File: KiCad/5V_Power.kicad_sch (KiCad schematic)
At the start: 24 parts, among them U4 NCP1117-3.3_SOT223, U5 XPS62912RPUR

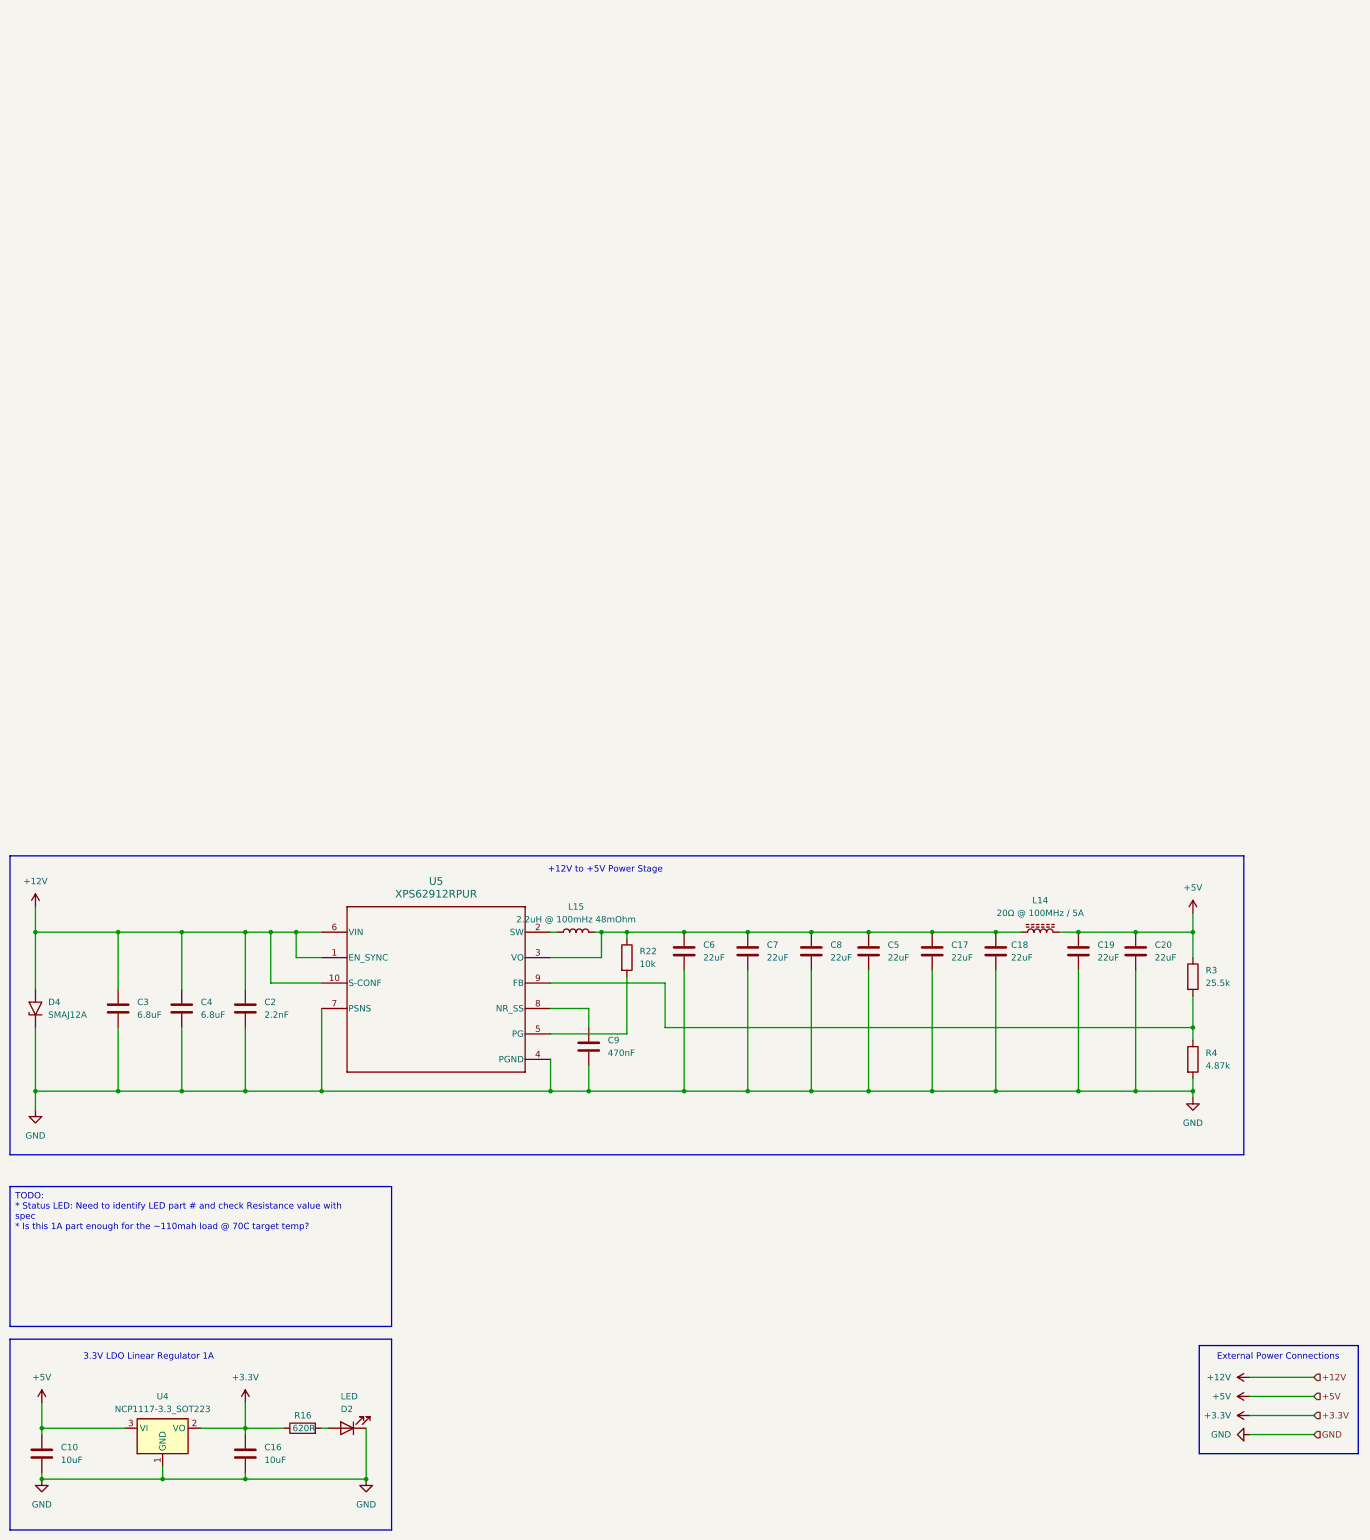
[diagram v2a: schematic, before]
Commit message: Convert Power to LDOs
Convert power section to use only LDOs. This means we will only get 4.75V or 4.5V on the analog line but this comes with greatly increased simplicity of layout.
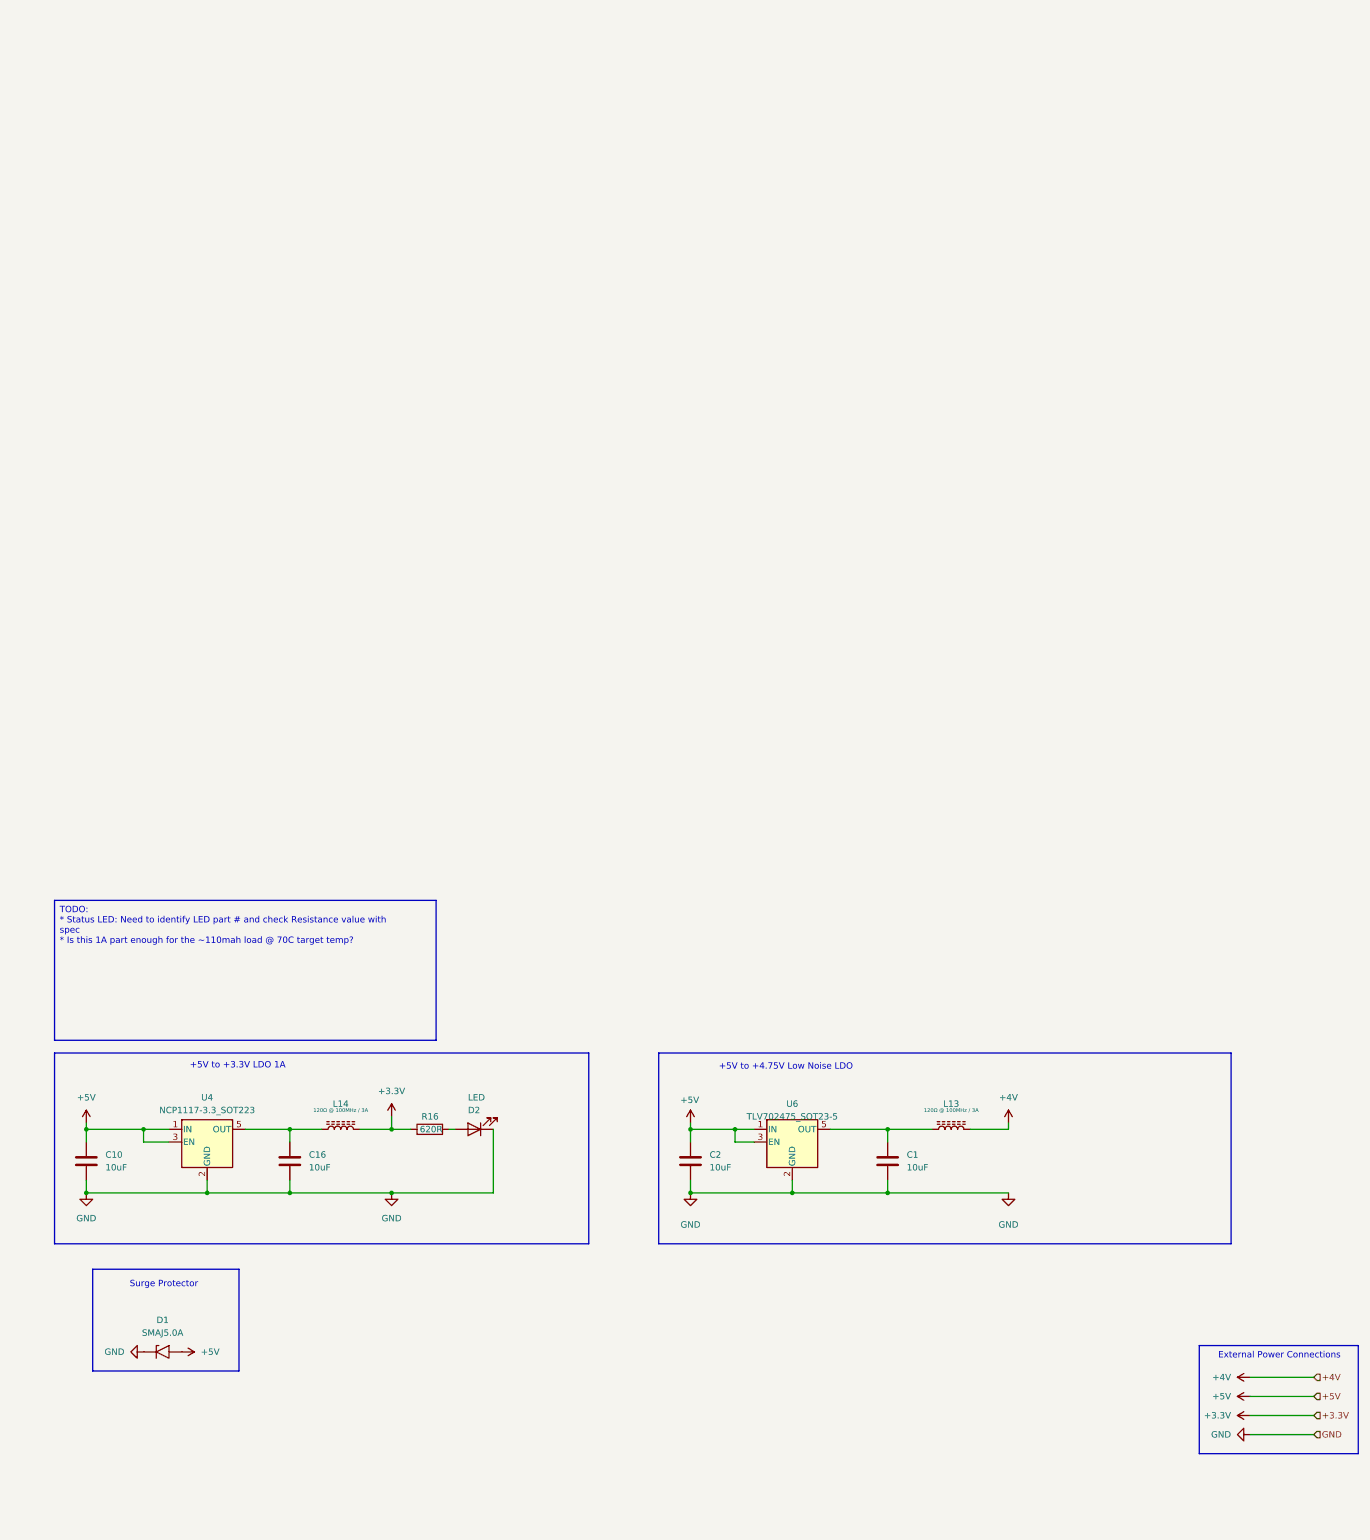
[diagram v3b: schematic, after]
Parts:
- removed C17, C18, C19, C20, C5, C6, C7, C8: 22uF, Capacitor_SMD:C_0805_2012Metric_Pad1.18x1.45mm_HandSolder, symbol Device:C
- removed C3, C4: 6.8uF, Capacitor_SMD:C_0805_2012Metric_Pad1.18x1.45mm_HandSolder, symbol Device:C
- removed C9: 470nF, Capacitor_SMD:C_0805_2012Metric_Pad1.18x1.45mm_HandSolder, symbol Device:C
- removed D4: SMAJ12A, Diode_SMD:D_SMA, symbol Diode:SMAJ12A
- removed L15: 2.2uH @ 100mHz 48mOhm, Inductor_SMD:L_Pulse_PA4320, symbol Device:L
- removed R22: 10k, Resistor_SMD:R_0805_2012Metric_Pad1.20x1.40mm_HandSolder, symbol Device:R
- removed R3: 25.5k, Resistor_SMD:R_0805_2012Metric_Pad1.20x1.40mm_HandSolder, symbol Device:R
- removed R4: 4.87k, Resistor_SMD:R_0805_2012Metric_Pad1.20x1.40mm_HandSolder, symbol Device:R
- removed U5: XPS62912RPUR, RPU0010A-MFG, symbol TPS62912:XPS62912RPUR
- added C1: 10uF, Capacitor_SMD:C_0805_2012Metric_Pad1.18x1.45mm_HandSolder, symbol Device:C
- added D1: SMAJ5.0A, Diode_SMD:D_SMA, symbol Diode:SMAJ5.0A
- added L13: 120Ω @ 100MHz / 3A, Inductor_SMD:L_0805_2012Metric_Pad1.05x1.20mm_HandSolder, symbol Device:L_Ferrite
- added U6: TLV702475_SOT23-5, Package_TO_SOT_SMD:SOT-23-5_HandSoldering, symbol Regulator_Linear:TLV702475_SOT23-5
- C2: value 2.2nF -> 10uF
- L14: value 20Ω @ 100MHz / 5A -> 120Ω @ 100MHz / 3A
- U4: footprint Package_TO_SOT_SMD:SOT-223-3_TabPin2 -> Package_TO_SOT_SMD:SOT-23-5; symbol Regulator_Linear:NCP1117-3.3_SOT223 -> Regulator_Linear:TLV70233_SOT23-5
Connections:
- net +12V is gone; now on net +5V: C2.1
- net +3.3V: now also L14.2; no longer C16.1, U4.2 (VO)
- net +5V: now also U4.1 (IN), D1.2 (A2), U6.1 (IN), U6.3 (EN); no longer L14.2
- net GND: now also U4.2 (GND), C1.2, D1.1 (A1), U6.2 (GND); no longer U4.1 (GND)
- net at L14.1: now also C16.1, U4.5 (OUT)
- new net: C1.1, L13.1, U6.5 (OUT)
- new net +4V: L13.2
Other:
- note added: "+5V to +3.3V LDO 1A"
- note added: "+5V to +4.75V Low Noise LDO"
- note added: "Surge Protector"
- note removed: "+12V to +5V Power Stage"
- note removed: "3.3V LDO Linear Regulator 1A"
- moved on the sheet: C10, C16, D2, R16

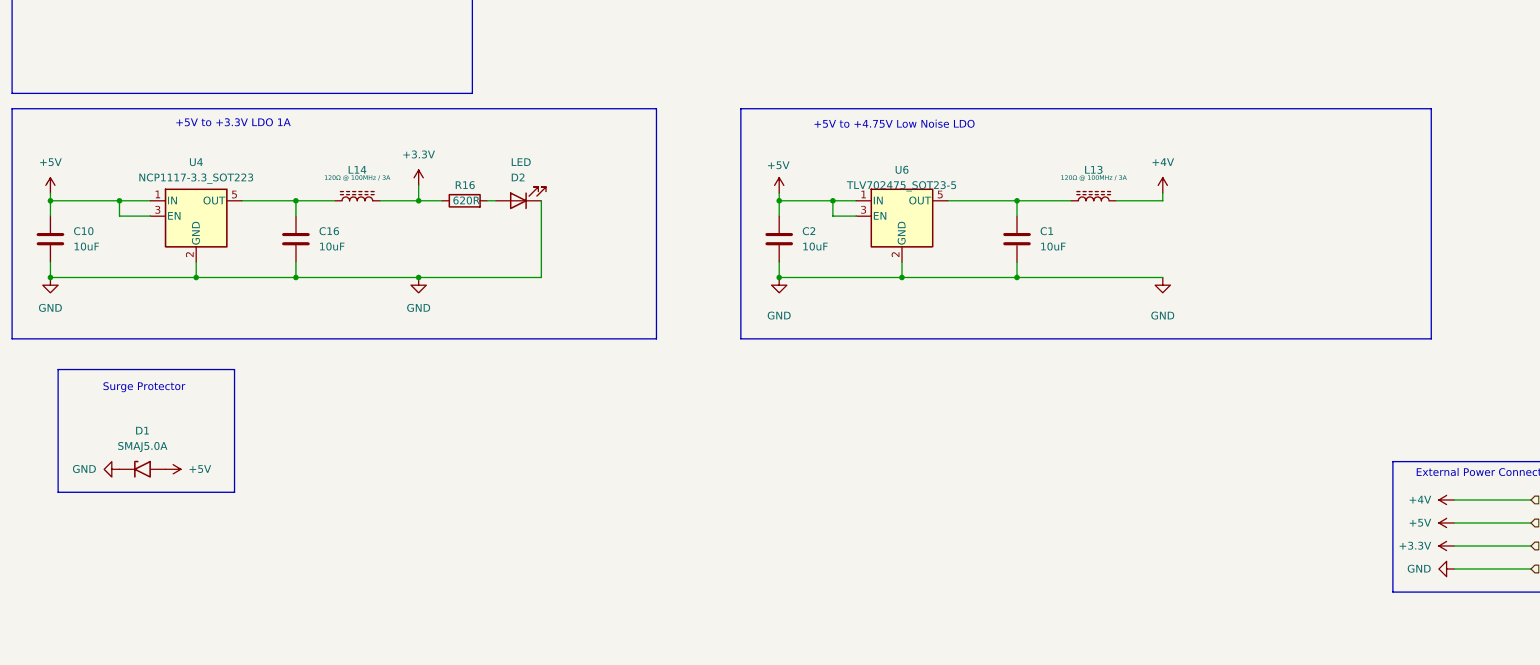
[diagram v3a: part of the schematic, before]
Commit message: Add Single Wire Debug
* Add Single Wire Debug (SWD) Tag Connect Connector
* Re-layout of 5V power so the 5V pins connect to a pad directly behind the USB connector
* Add 0R resistors to air gap the 3.3V and 5V power rails for incremental board bringup
* Rotate ADS1220 for cleaner layout
* Remove connections to reference voltage pins, since AVDD/AVSS is a valid reference

fixup

fixup

fixup
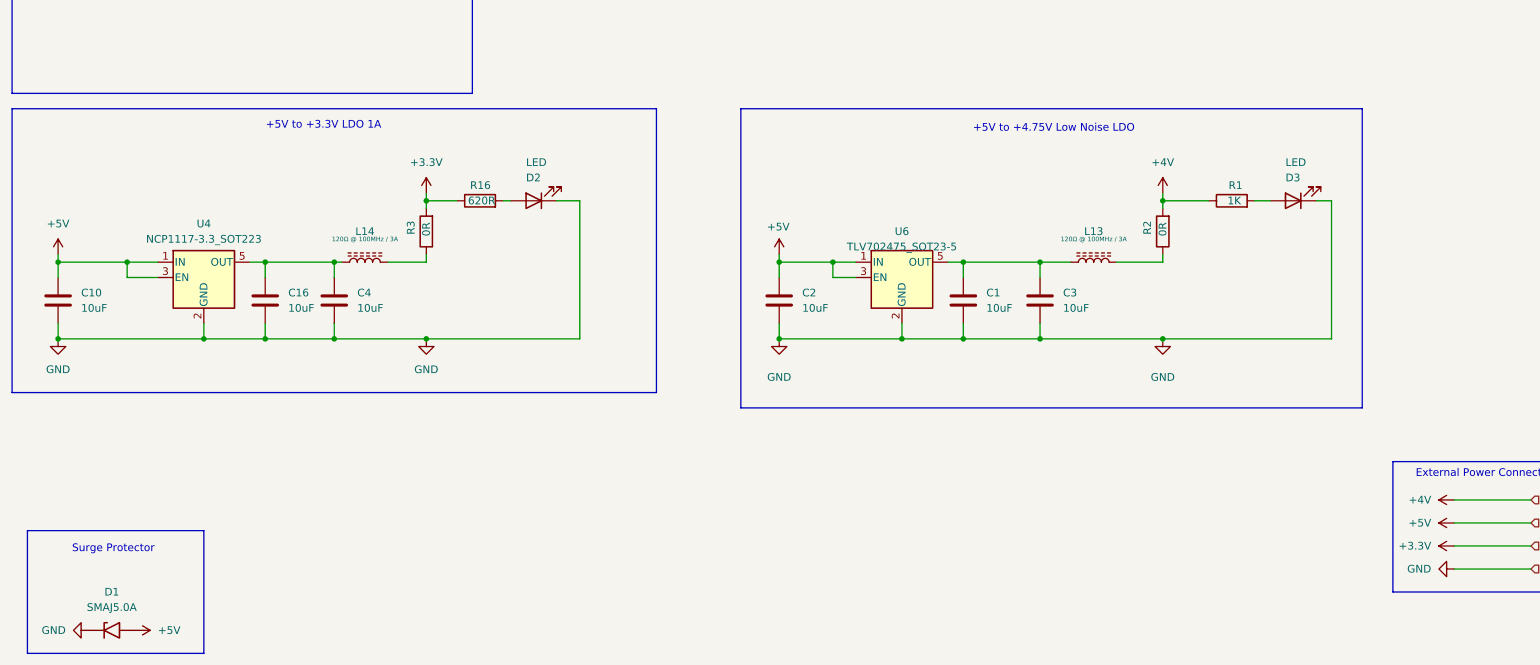
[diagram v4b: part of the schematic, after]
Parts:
- added C3, C4: 10uF, Capacitor_SMD:C_0805_2012Metric_Pad1.18x1.45mm_HandSolder, symbol Device:C
- added D3: LED, LED_SMD:LED_1206_3216Metric_Pad1.42x1.75mm_HandSolder, symbol Device:LED
- added R1: 1K, Resistor_SMD:R_0805_2012Metric_Pad1.20x1.40mm_HandSolder, symbol Device:R
- added R2, R3: 0R, Resistor_SMD:R_0805_2012Metric_Pad1.20x1.40mm_HandSolder, symbol Device:R
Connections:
- net +3.3V: now also R3.2; no longer L14.2
- net +4V: now also R1.1, R2.2; no longer L13.2
- net GND: now also C3.2, C4.2, D3.1 (K)
- net at C16.1, L14.1, U4.5 (OUT): now also C4.1
- net at C1.1, L13.1, U6.5 (OUT): now also C3.1
- new net: L13.2, R2.1
- new net: D3.2 (A), R1.2
- new net: L14.2, R3.1
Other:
- moved on the sheet: C1, C10, C16, C2, D1, D2, L13, L14, R16, U4, U6
